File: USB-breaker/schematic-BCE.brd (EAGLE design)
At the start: 67.5 x 45.5 mm, 23 parts, among them K1 G6K-2P, K2 G6K-2P, T1 2PA733, T2 2SC945, X1 PN61729-S, X2 PN87520-S, X3 10104110, X4 UX60SC-MB-5ST

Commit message: Value of R1 changed from 120 Ω to 100 Ω. Otherwise the voltage for relay K1 is too low.
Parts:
- R1: value 120 -> 100
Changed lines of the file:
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@@
 </autorouter>
 <elements>
-<element name="R1" library="resistor" package="0207/10" value="120" x="34.29" y="43.18" smashed="yes" rot="R180">
+<element name="R1" library="resistor" package="0207/10" value="100" x="34.29" y="43.18" smashed="yes" rot="R180">
 <attribute name="NAME" x="31.623" y="42.291" size="1.27" layer="25" ratio="10" rot="R180"/>
 <attribute name="VALUE" x="36.5506" y="43.815" size="1.27" layer="27" ratio="10" rot="R180"/>

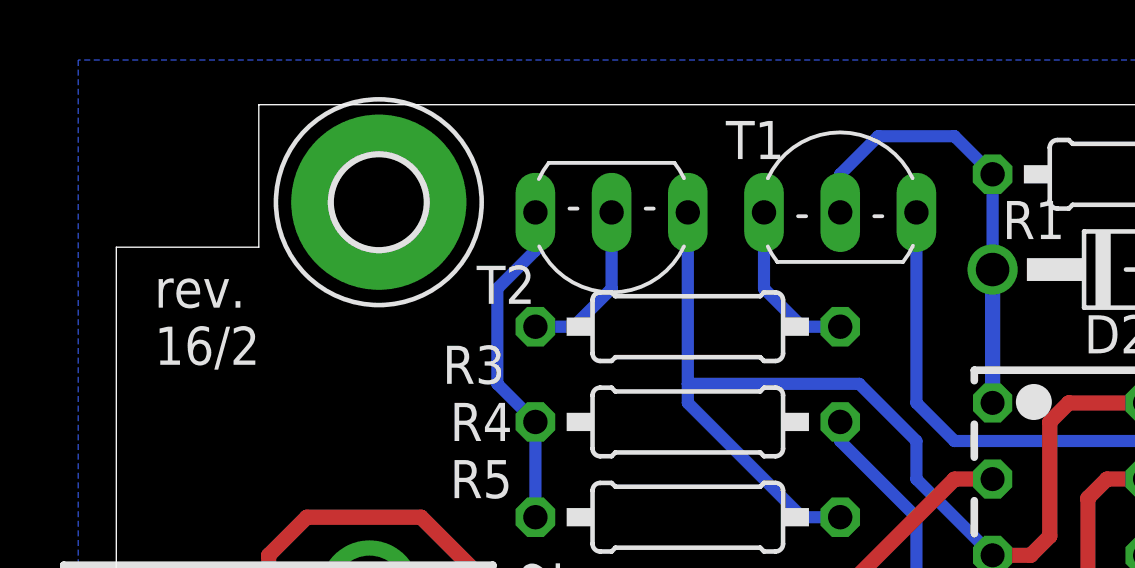
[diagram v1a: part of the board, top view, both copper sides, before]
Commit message: T1 is now used from another library. BCE was wrong, ECB is the right package.
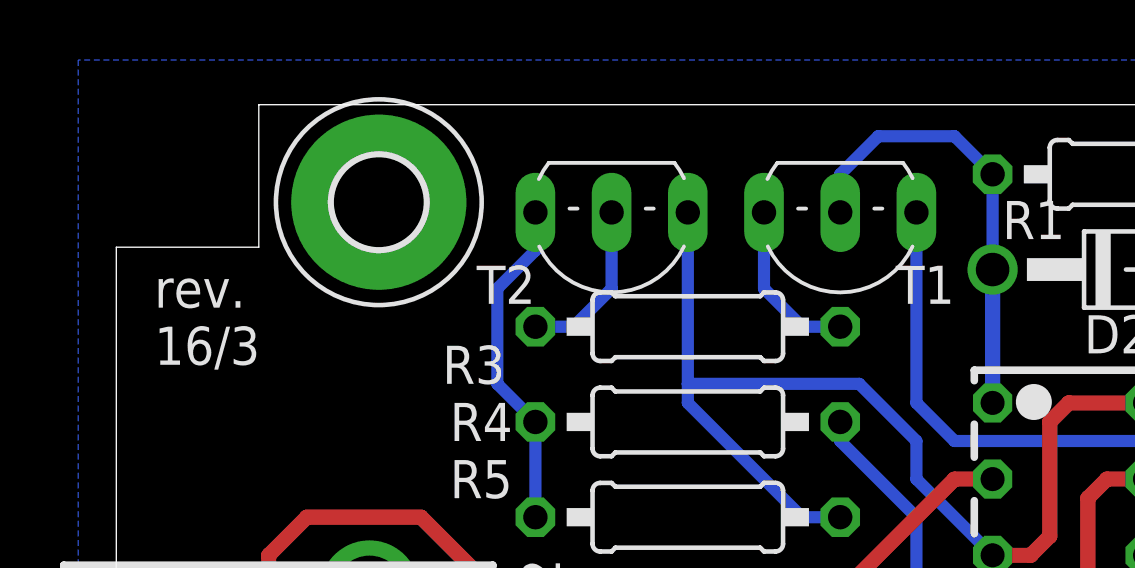
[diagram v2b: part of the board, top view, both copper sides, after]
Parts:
- T1: device transistor:TO92-BCE -> mibe:TO92-ECB
- turned T1 to 180 degrees
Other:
- board text added: "rev. 16/3"
- board text removed: "rev. 16/2"
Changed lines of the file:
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@@
 <text x="30.48" y="11.43" size="2.25" layer="21" ratio="10">USB-Breaker</text>
 <text x="1.27" y="36.83" size="1.27" layer="21" ratio="10">rev.
-16/2</text>
+16/3</text>
 <text x="51.435" y="0.635" size="1" layer="21" ratio="10">top</text>
 <text x="53.975" y="0.635" size="1" layer="22" ratio="10" rot="MR0">bottom</text>
@@
 <attribute name="VALUE" x="10.795" y="8.89" size="1.27" layer="27" rot="R270"/>
 </element>
-<element name="T1" library="transistor" package="TO92-BCE" value="2PA733" x="24.13" y="41.91" smashed="yes">
-<attribute name="NAME" x="20.32" y="43.688" size="1.27" layer="25" ratio="10"/>
-<attribute name="VALUE" x="21.59" y="37.338" size="1.27" layer="27" ratio="10"/>
+<element name="T1" library="mibe" package="TO92-ECB" value="2PA733" x="24.13" y="41.91" smashed="yes" rot="R180">
+<attribute name="NAME" x="27.94" y="40.132" size="1.27" layer="25" ratio="10" rot="R180"/>
+<attribute name="VALUE" x="26.67" y="46.482" size="1.27" layer="27" ratio="10" rot="R180"/>
 </element>
 <element name="R3" library="resistor" package="0207/10" value="2k7" x="19.05" y="38.1" smashed="yes">
